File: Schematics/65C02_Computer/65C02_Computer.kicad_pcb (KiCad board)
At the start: 2 copper layers, 203.2 x 149.9 mm, 65 parts, among them J1 CLK Jumper, J10 LCD Connector, J2 Optional UART Port, J3 USB_B_Micro, J4 USB_B, J5 Power Connector, J6 Mini-DIN-6, J7 Expansion port, J8 VIA2PA, J9 VIA2PB, SW1 RESET, U1 74HC21, U10 ATtiny4313-PU, U11 65C22S, U12 65C22S, U2 74HC00, U3 74HC02, U4 NE555, U5 65C51N, U6 FT230XS, U7 65C02S, U8 28C256, U9 62256, X1 1MHz, X2 1.8432MHz

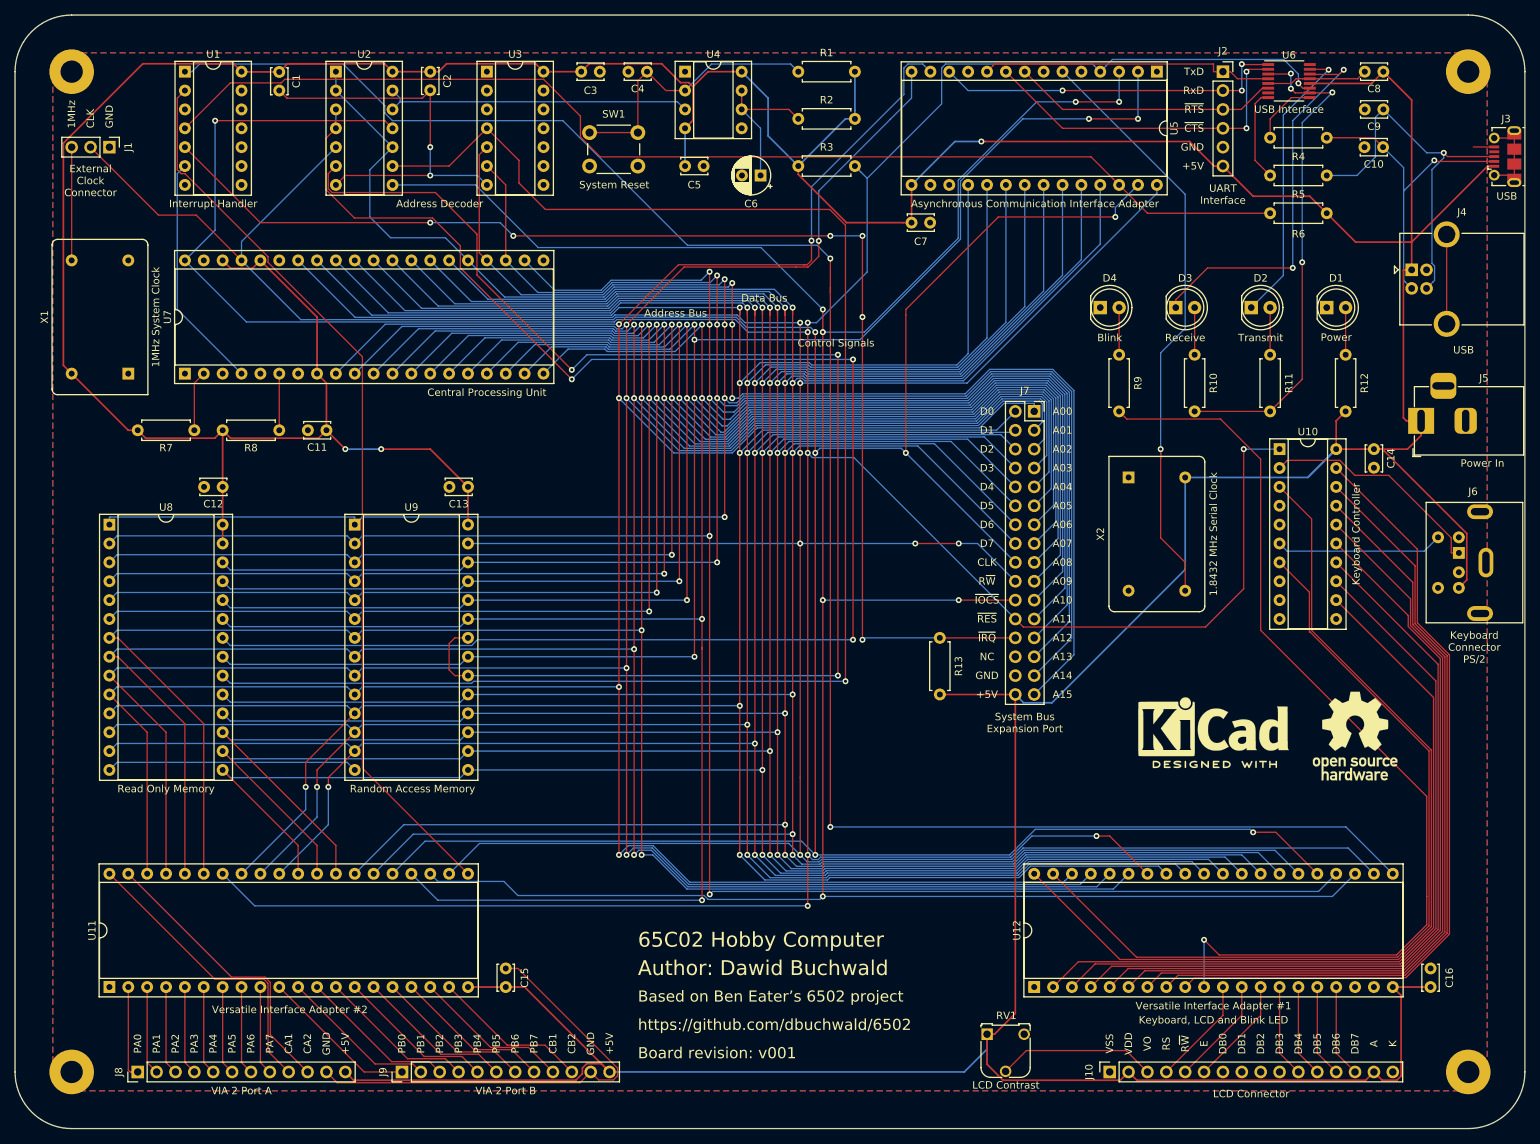
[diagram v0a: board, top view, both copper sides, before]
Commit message: Added ferrite bead, got rid of DRC errors, other changes
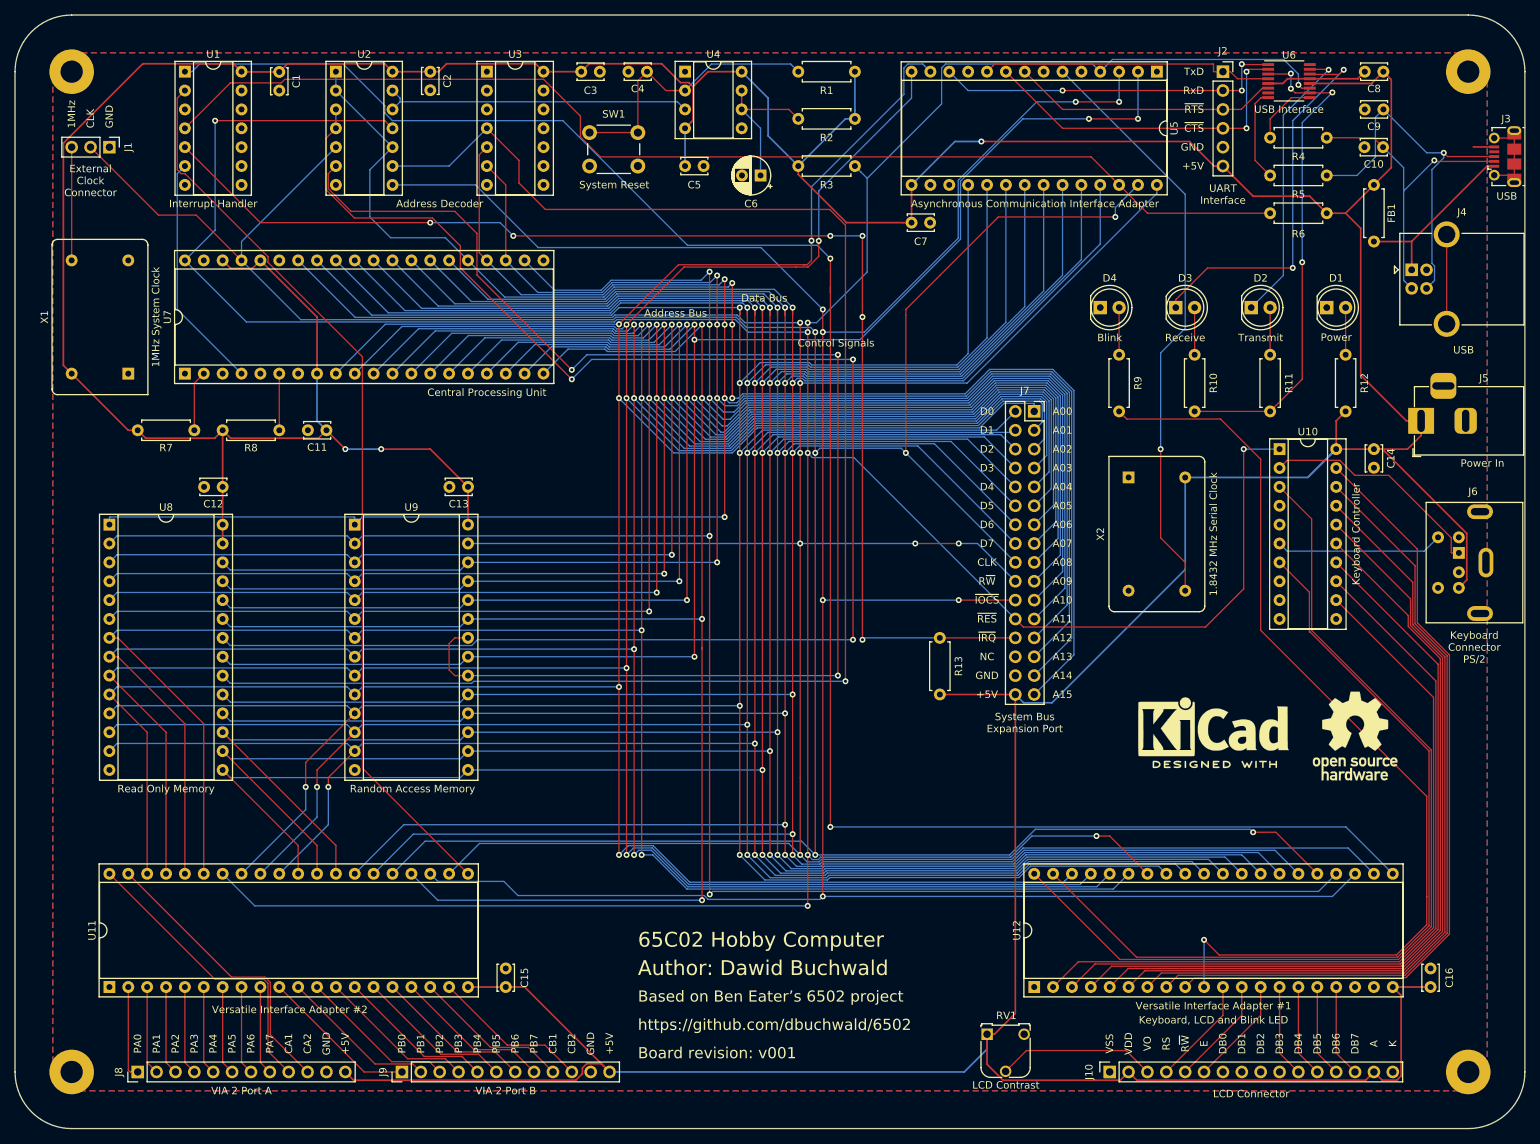
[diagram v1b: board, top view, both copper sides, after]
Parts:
- added FB1: Ferrite_Bead_Small, Resistor_THT:R_Axial_DIN0207_L6.3mm_D2.5mm_P7.62mm_Horizontal, F.Cu at (200.7, 43.2)
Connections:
- J3 pad 1: +5V -> Net-(FB1-Pad2)
- J4 pad 1: +5V -> Net-(FB1-Pad2)
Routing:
- net GND: track 167.0 -> 16.7 mm, vias 2 -> 0
- net Net-(FB1-Pad2): track 0.00 -> 24.2 mm
- net +5V: track 837.6 -> 815.3 mm
- net RS232CLK: track 80.7 -> 79.4 mm

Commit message: Improved 65C02 PCB
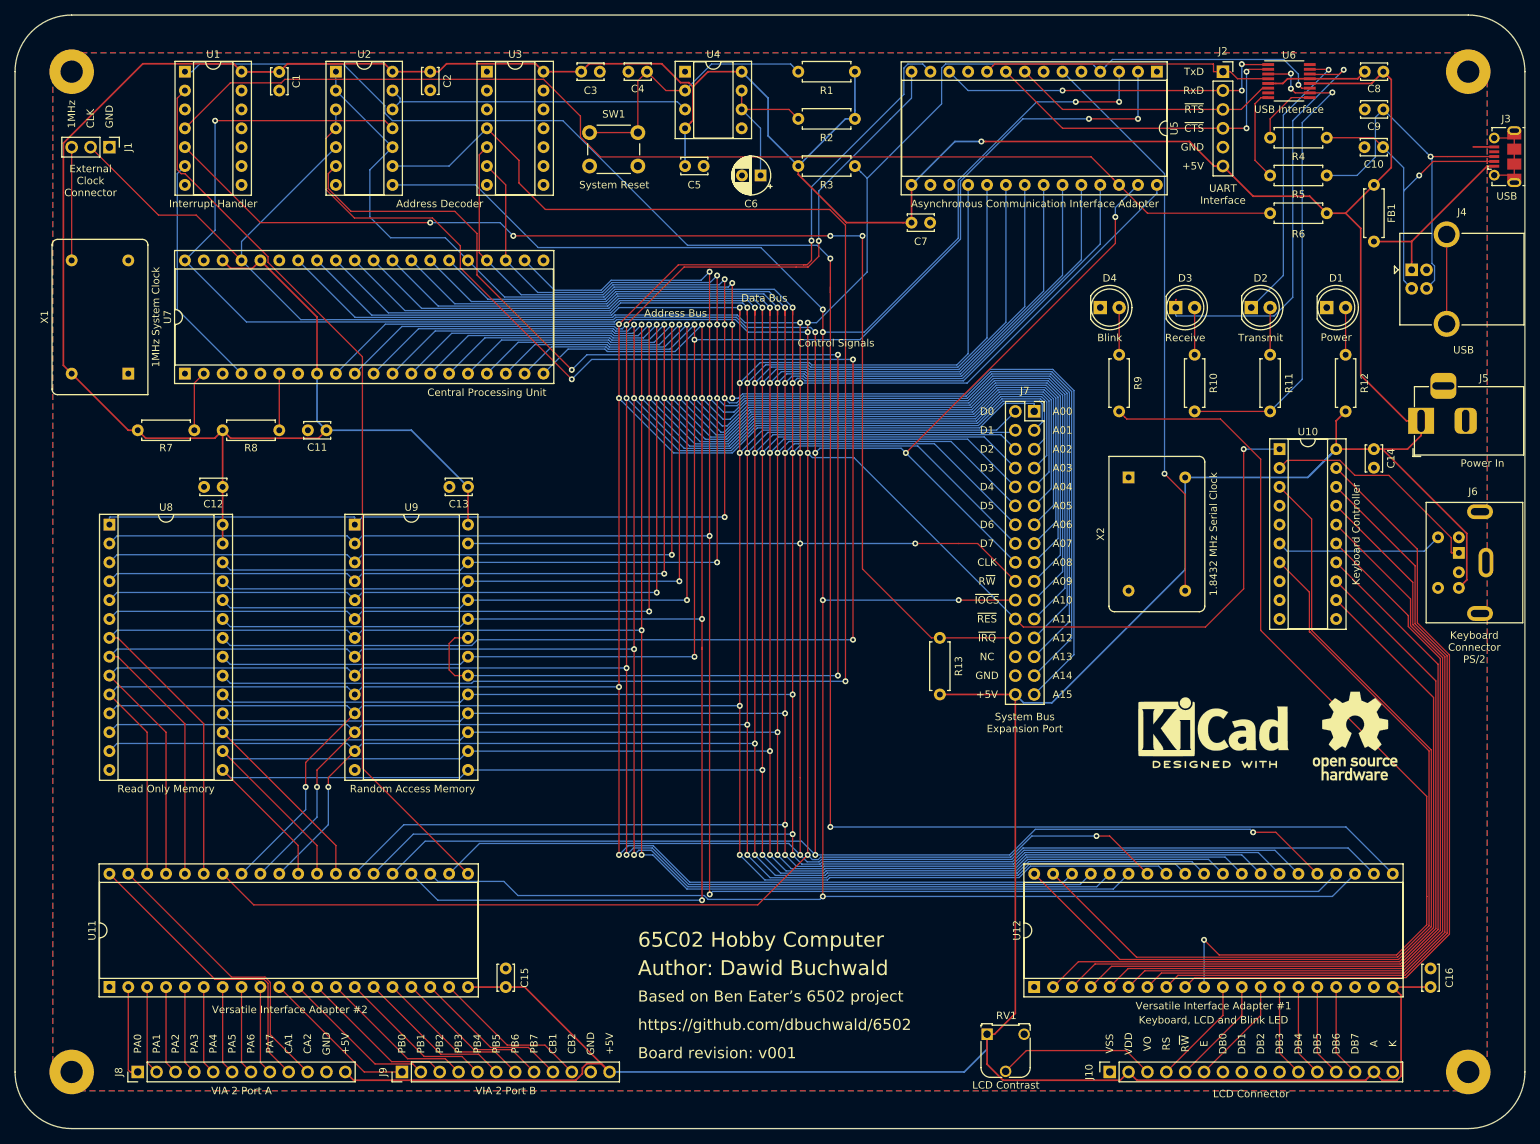
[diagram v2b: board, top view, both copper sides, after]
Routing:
- net CLK: track 421.9 -> 412.7 mm
- net ~IRQX: track 171.2 -> 165.4 mm, vias 6 -> 4
- net Net-(D3-Pad1): track 53.2 -> 57.5 mm, vias 2 -> 1
- net ~RES: track 533.4 -> 529.3 mm, vias 9 -> 8
- net RS232CLK: track 79.4 -> 76.7 mm
- net PUSBD+: track 51.5 -> 50.4 mm
- net +5V: vias 3 -> 1
- net Net-(R10-Pad1): vias 4 -> 3
- net R~W: vias 7 -> 6

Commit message: Added AVR ISP interface
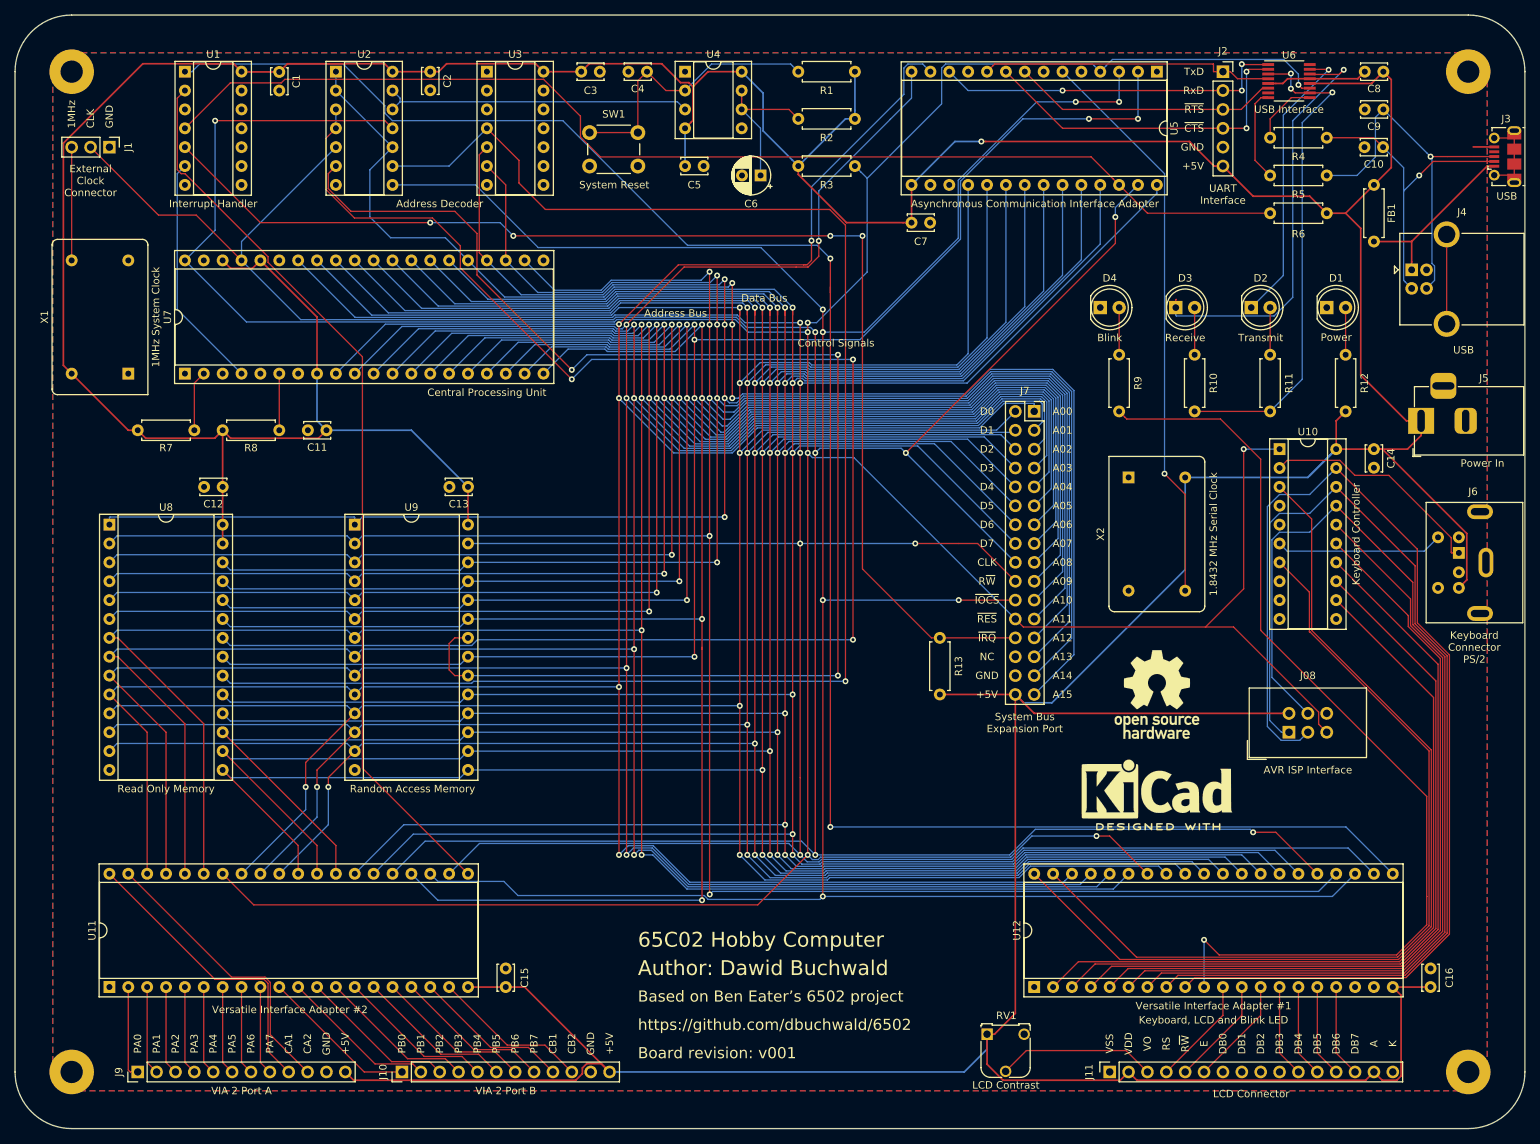
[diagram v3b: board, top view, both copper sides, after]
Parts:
- added J08: AVR-ISP-6, Connector_IDC:IDC-Header_2x03_P2.54mm_Vertical, F.Cu at (189.2, 116.8)
- R3: value 1K -> 10K
- moved REF** 27.2 mm to (171.4, 111.8)
- moved REF** 11.3 mm to (171.4, 124.5)
- renumbered J9 to J10, J10 to J11, J8 to J9
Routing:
- net /6502 Peripherals/v1pa7: track 107.6 -> 155.2 mm
- net /6502 Peripherals/v1pa6: track 107.1 -> 147.8 mm
- net +5V: track 815.3 -> 853.2 mm
- net /6502 Peripherals/v1pa5: track 106.5 -> 142.5 mm
- net ~RES: track 529.3 -> 552.4 mm
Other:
- board text added: "AVR ISP Interface"

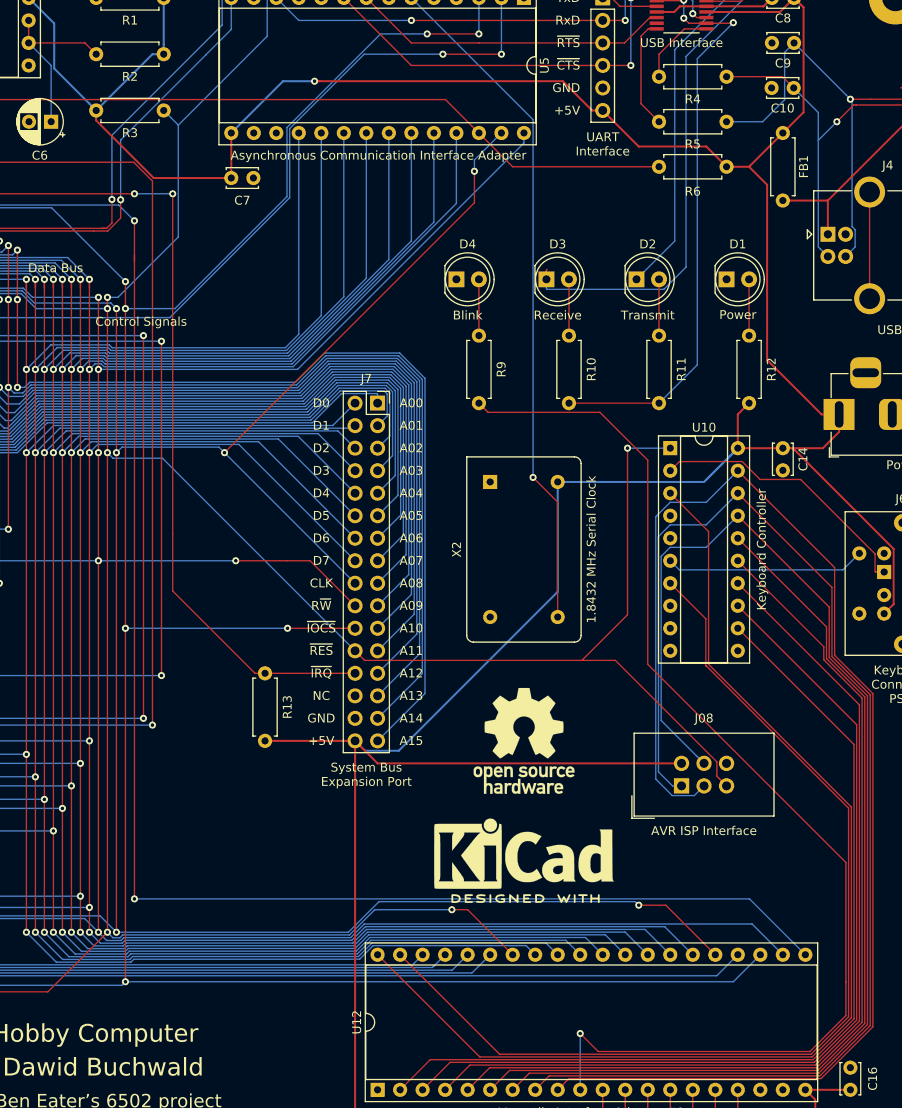
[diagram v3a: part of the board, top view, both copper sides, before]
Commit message: Changed AVR ISP port to 10-pin
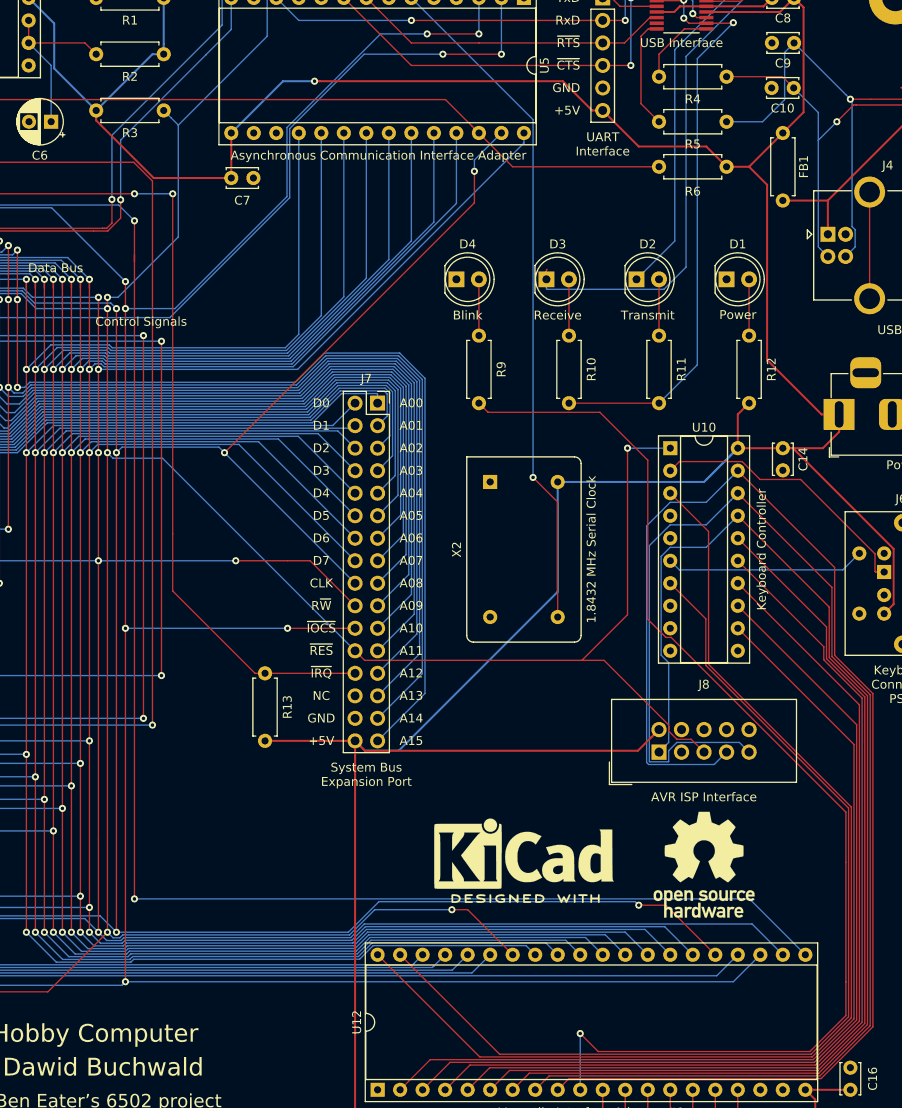
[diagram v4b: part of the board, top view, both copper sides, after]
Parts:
- removed J08: AVR-ISP-6, Connector_IDC:IDC-Header_2x03_P2.54mm_Vertical
- added J8: AVR-ISP-10, Connector_IDC:IDC-Header_2x05_P2.54mm_Vertical, F.Cu at (186.7, 113.0)
- moved REF** 24.7 mm to (191.8, 125.7)
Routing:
- net /6502 Peripherals/v1pa6: track 147.8 -> 157.2 mm
- net ~RES: track 552.4 -> 547.8 mm
- net /6502 Peripherals/v1pa5: track 142.5 -> 140.0 mm
- net +5V: track 853.2 -> 851.1 mm
- net /6502 Peripherals/v1pa7: track 155.2 -> 156.8 mm
